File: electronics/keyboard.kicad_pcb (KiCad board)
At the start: 2 copper layers, 243 parts, among them CON1 AVR-ISP-6, J2 CONN_01X02_FEMALE, Q1 Q_NMOS_DGS, Q2 Q_NMOS_DGS, Q3 Q_PMOS_DGS, Q4 Q_NMOS_DGS, Q5 Q_PMOS_DGS, SW1 SW_DPST, SW10 SW_Push, SW11 SW_Push, SW12 SW_Push, SW13 SW_Push, SW14 SW_Push, SW15 SW_Push, SW16 SW_Push, SW17 SW_Push, SW18 SW_Push, SW19 SW_Push, SW2 SW_Push, SW20 SW_Push, SW21 SW_Push, SW22 SW_Push, SW23 SW_Push, SW24 SW_Push, SW25 SW_Push, SW26 SW_Push, SW27 SW_Push, SW28 SW_Push, SW29 SW_Push, SW3 SW_Push, SW30 SW_Push, SW31 SW_Push, SW32 SW_Push, SW33 SW_Push, SW34 SW_Push, SW35 SW_Push, SW36 SW_Push, SW37 SW_Push, SW38 SW_Push, SW39 SW_Push, SW4 SW_Push, SW40 SW_Push, SW41 SW_Push, SW42 SW_Push, SW43 SW_Push, SW44 SW_Push, SW45 SW_Push, SW46 SW_Push, SW47 SW_Push, SW48 SW_Push, SW49 SW_Push, SW5 SW_Push, SW50 SW_Push, SW51 SW_Push, SW52 SW_Push, SW53 SW_Push, SW54 SW_Push, SW55 SW_Push, SW56 SW_Push, SW57 SW_Push, SW58 SW_Push, SW59 SW_Push, SW6 SW_Push, SW60 SW_Push, SW61 SW_Push, SW62 SW_Push, SW63 SW_Push, SW64 SW_Push, SW65 SW_Push, SW66 SW_Push, SW67 SW_Push, SW68 SW_Push, SW69 SW_Push, SW7 SW_Push, SW70 SW_Push, SW71 SW_Push, SW72 SW_Push, SW73 SW_Push, SW74 SW_Push, SW75 SW_Push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

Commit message: Seperated elements in a sane way...
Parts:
- moved U2 181.8 mm to (325.1, 113.0)
- moved R15 176.2 mm to (340.4, 110.5)
- moved R18 161.5 mm to (340.4, 102.9)
- moved R17 161.5 mm to (349.2, 102.9)
- moved Q2 158.0 mm to (306.1, 124.5)
- moved R14 157.7 mm to (306.1, 129.5), turned to 180 degrees
- moved R16 157.4 mm to (304.8, 110.5)
- moved D1 156.7 mm to (350.5, 115.6)
- moved D2 156.7 mm to (350.5, 111.8)
- moved R5 143.5 mm to (301.0, 102.9)
- moved C9 142.2 mm to (323.9, 171.4)
- moved R13 126.4 mm to (308.6, 88.9)
- moved R8 117.4 mm to (302.3, 82.5)
- moved Q1 113.7 mm to (303.5, 99.1)
- moved R11 112.5 mm to (308.6, 78.7)
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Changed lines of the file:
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@@
     (links 407)
     (no_connects 407)
-    (area -421.280001 -139.340001 341.665001 243.975)
+    (area -421.280001 -139.340001 401.245001 243.975)
     (thickness 1.6)
     (drawings 0)
@@
   )
   (module Capacitors_SMD:C_0805_HandSoldering (layer F.Cu)
-    (at 187.96 129.54)
+    (at 323.85 171.45)
     (descr "Capacitor SMD 0805, hand soldering")
     (tags "capacitor 0805")
@@
   )
   (module LEDs:LED_0805 (layer F.Cu)
-    (at 200.66 161.29)
+    (at 350.52 115.57)
     (descr "LED 0805 smd package")
     (tags "LED led 0805 SMD smd SMT smt smdled SMDLED smtled SMTLED")
@@
   )
   (module LEDs:LED_0805 (layer F.Cu)
-    (at 200.66 157.48)
+    (at 350.52 111.76)
     (descr "LED 0805 smd package")
     (tags "LED led 0805 SMD smd SMT smt smdled SMDLED smtled SMTLED")
@@
   )
   (module TO_SOT_Packages_SMD:SC-59 (layer F.Cu)
-    (at 190.5 86.36)
+    (at 303.53 99.06)
     (descr "SC-59, https://lib.chipdip.ru/images/import_diod/original/SOT-23_SC-59.jpg")
     (tags SC-59)
@@
   )
   (module TO_SOT_Packages_SMD:SC-59 (layer F.Cu)
-    (at 152.4 87.63)
+    (at 306.07 124.46)
     (descr "SC-59, https://lib.chipdip.ru/images/import_diod/original/SOT-23_SC-59.jpg")
     (tags SC-59)
@@
   )
   (module Resistors_SMD:R_0805_HandSoldering (layer F.Cu)
-    (at 157.48 104.14)
+    (at 300.99 102.87)
     (descr "Resistor SMD 0805, hand soldering")
     (tags "resistor 0805")
@@
   )
   (module Resistors_SMD:R_0805_HandSoldering (layer F.Cu)
-    (at 196.85 81.28)
+    (at 306.07 102.87)
     (descr "Resistor SMD 0805, hand soldering")
     (tags "resistor 0805")
@@
   )
   (module Resistors_SMD:R_0805_HandSoldering (layer F.Cu)
-    (at 199.39 95.25)
+    (at 308.61 82.55)
     (descr "Resistor SMD 0805, hand soldering")
     (tags "resistor 0805")
@@
   )
   (module Resistors_SMD:R_0805_HandSoldering (layer F.Cu)
-    (at 185.42 93.98)
+    (at 302.26 82.55)
     (descr "Resistor SMD 0805, hand soldering")
     (tags "resistor 0805")
@@
   )
   (module Resistors_SMD:R_0805_HandSoldering (layer F.Cu)
-    (at 203.2 87.63)
+    (at 306.07 118.11)
     (descr "Resistor SMD 0805, hand soldering")
     (tags "resistor 0805")
@@
   )
   (module Resistors_SMD:R_0805_HandSoldering (layer F.Cu)
-    (at 207.01 107.95)
+    (at 302.26 78.74)
     (descr "Resistor SMD 0805, hand soldering")
     (tags "resistor 0805")
@@
   )
   (module Resistors_SMD:R_0805_HandSoldering (layer F.Cu)
-    (at 218.44 146.05)
+    (at 308.61 78.74)
     (descr "Resistor SMD 0805, hand soldering")
     (tags "resistor 0805")
@@
   )
   (module Resistors_SMD:R_0805_HandSoldering (layer F.Cu)
-    (at 212.09 146.05)
+    (at 302.26 88.9)
     (descr "Resistor SMD 0805, hand soldering")
     (tags "resistor 0805")
@@
   )
   (module Resistors_SMD:R_0805_HandSoldering (layer F.Cu)
-    (at 210.82 168.91)
+    (at 308.61 88.9)
     (descr "Resistor SMD 0805, hand soldering")
     (tags "resistor 0805")
@@
   )
   (module Resistors_SMD:R_0805_HandSoldering (layer F.Cu)
-    (at 149.86 151.13)
+    (at 306.07 129.54 180)
     (descr "Resistor SMD 0805, hand soldering")
     (tags "resistor 0805")
     (attr smd)
-    (fp_text reference R14 (at 0 -1.7) (layer F.SilkS)
+    (fp_text reference R14 (at 0 -1.7 180) (layer F.SilkS)
       (effects (font (size 1 1) (thickness 0.15)))
     )
-    (fp_text value 10k (at 0 1.75) (layer F.Fab)
+    (fp_text value 10k (at 0 1.75 180) (layer F.Fab)
       (effects (font (size 1 1) (thickness 0.15)))
     )
-    (fp_text user %R (at 0 -1.7) (layer F.Fab)
+    (fp_text user %R (at 0 -1.7 180) (layer F.Fab)
       (effects (font (size 1 1) (thickness 0.15)))
     )
@@
     (fp_line (start 2.35 0.9) (end 2.35 -0.9) (layer F.CrtYd) (width 0.05))
     (fp_line (start 2.35 0.9) (end -2.35 0.9) (layer F.CrtYd) (width 0.05))
-    (pad 1 smd rect (at -1.35 0) (size 1.5 1.3) (layers F.Cu F.Paste F.Mask)
+    (pad 1 smd rect (at -1.35 0 180) (size 1.5 1.3) (layers F.Cu F.Paste F.Mask)
       (net 3 +5V))
-    (pad 2 smd rect (at 1.35 0) (size 1.5 1.3) (layers F.Cu F.Paste F.Mask)
+    (pad 2 smd rect (at 1.35 0 180) (size 1.5 1.3) (layers F.Cu F.Paste F.Mask)
       (net 122 /PF1))
     (model Resistors_SMD.3dshapes/R_0805.wrl
@@
   )
   (module Resistors_SMD:R_0805_HandSoldering (layer F.Cu)
-    (at 168.91 151.13)
+    (at 340.36 110.49)
     (descr "Resistor SMD 0805, hand soldering")
     (tags "resistor 0805")
@@
   )
   (module Resistors_SMD:R_0805_HandSoldering (layer F.Cu)
-    (at 149.86 138.43)
+    (at 304.8 110.49)
     (descr "Resistor SMD 0805, hand soldering")
     (tags "resistor 0805")
@@
   )
   (module Resistors_SMD:R_0805_HandSoldering (layer F.Cu)
-    (at 194.31 148.59)
+    (at 349.25 102.87)
     (descr "Resistor SMD 0805, hand soldering")
     (tags "resistor 0805")
@@
   )
   (module Resistors_SMD:R_0805_HandSoldering (layer F.Cu)
-    (at 185.42 148.59)
+    (at 340.36 102.87)
     (descr "Resistor SMD 0805, hand soldering")
     (tags "resistor 0805")
@@
   )
   (module RF_Modules:RN42 (layer F.Cu)
-    (at 156.21 180.34)
+    (at 325.12 113.03)
     (descr "Class 2 Bluetooth Module with on-board antenna")
     (tags "Bluetooth Module")

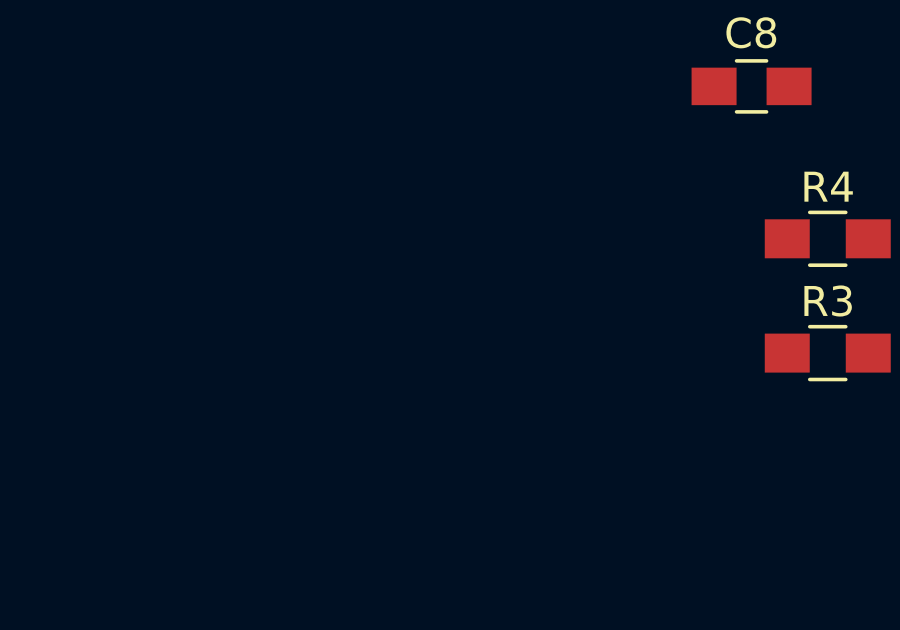
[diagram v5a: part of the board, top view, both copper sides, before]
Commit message: Updated the usb connector to micro usb at the momement because it is in the lib
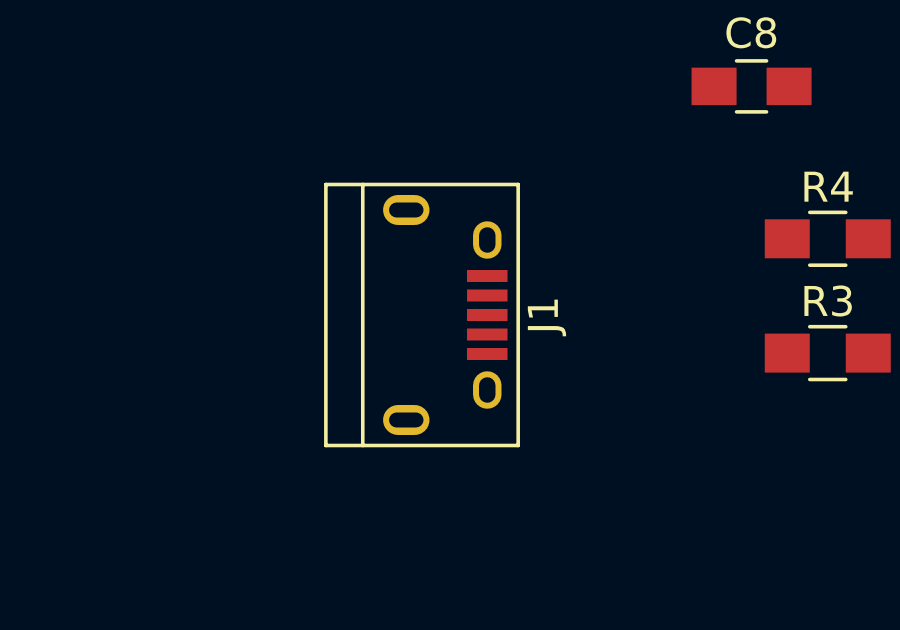
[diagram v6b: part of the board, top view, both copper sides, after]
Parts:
- added J1: USB_OTG, Connectors:USB_Micro-B, F.Cu at (295.9, 186.7)
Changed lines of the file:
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@@
 (kicad_pcb (version 4) (host pcbnew 4.0.6)
   (general
-    (links 407)
-    (no_connects 407)
-    (area -421.280001 -139.340001 401.245001 243.975)
+    (links 415)
+    (no_connects 415)
+    (area 0 0 0 0)
     (thickness 1.6)
     (drawings 0)
     (tracks 0)
     (zones 0)
-    (modules 243)
-    (nets 195)
+    (modules 244)
+    (nets 196)
   )
   (page A4)
@@
   (net 193 "Net-(U4-Pad3)")
   (net 194 "Net-(CON1-Pad2)")
+  (net 195 "Net-(J1-Pad4)")
   (net_class Default "This is the default net class."
     (clearance 0.2)
@@
     (add_net "Net-(D95-Pad2)")
     (add_net "Net-(D96-Pad2)")
+    (add_net "Net-(J1-Pad4)")
     (add_net "Net-(Q3-Pad2)")
     (add_net "Net-(Q4-Pad1)")
@@
     )
   )
+  (module Connectors:USB_Micro-B (layer F.Cu)
+    (at 295.91 186.69 270)
+    (descr "Micro USB Type B Receptacle")
+    (tags "USB USB_B USB_micro USB_OTG")
+    (attr smd)
+    (fp_text reference J1 (at 0 -3.24 270) (layer F.SilkS)
+      (effects (font (size 1 1) (thickness 0.15)))
+    )
+    (fp_text value USB_OTG (at 0 5.01 270) (layer F.Fab)
+      (effects (font (size 1 1) (thickness 0.15)))
+    )
+    (fp_line (start -4.6 -2.59) (end 4.6 -2.59) (layer F.CrtYd) (width 0.05))
+    (fp_line (start 4.6 -2.59) (end 4.6 4.26) (layer F.CrtYd) (width 0.05))
+    (fp_line (start 4.6 4.26) (end -4.6 4.26) (layer F.CrtYd) (width 0.05))
+    (fp_line (start -4.6 4.26) (end -4.6 -2.59) (layer F.CrtYd) (width 0.05))
+    (fp_line (start -4.35 4.03) (end 4.35 4.03) (layer F.SilkS) (width 0.12))
+    (fp_line (start -4.35 -2.38) (end 4.35 -2.38) (layer F.SilkS) (width 0.12))
+    (fp_line (start 4.35 -2.38) (end 4.35 4.03) (layer F.SilkS) (width 0.12))
+    (fp_line (start 4.35 2.8) (end -4.35 2.8) (layer F.SilkS) (width 0.12))
+    (fp_line (start -4.35 4.03) (end -4.35 -2.38) (layer F.SilkS) (width 0.12))
+    (pad 1 smd rect (at -1.3 -1.35) (size 1.35 0.4) (layers F.Cu F.Paste F.Mask)
+      (net 10 /VBUS))
+    (pad 2 smd rect (at -0.65 -1.35) (size 1.35 0.4) (layers F.Cu F.Paste F.Mask)
+      (net 133 /DMINUS))
+    (pad 3 smd rect (at 0 -1.35) (size 1.35 0.4) (layers F.Cu F.Paste F.Mask)
+      (net 131 /DPLUS))
+    (pad 4 smd rect (at 0.65 -1.35) (size 1.35 0.4) (layers F.Cu F.Paste F.Mask)
+      (net 195 "Net-(J1-Pad4)"))
+    (pad 5 smd rect (at 1.3 -1.35) (size 1.35 0.4) (layers F.Cu F.Paste F.Mask)
+      (net 2 GND))
+    (pad 6 thru_hole oval (at -2.5 -1.35) (size 0.95 1.25) (drill oval 0.55 0.85) (layers *.Cu *.Mask)
+      (net 2 GND))
+    (pad 6 thru_hole oval (at 2.5 -1.35) (size 0.95 1.25) (drill oval 0.55 0.85) (layers *.Cu *.Mask)
+      (net 2 GND))
+    (pad 6 thru_hole oval (at -3.5 1.35) (size 1.55 1) (drill oval 1.15 0.5) (layers *.Cu *.Mask)
+      (net 2 GND))
+    (pad 6 thru_hole oval (at 3.5 1.35) (size 1.55 1) (drill oval 1.15 0.5) (layers *.Cu *.Mask)
+      (net 2 GND))
+  )
 )

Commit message: Started working on the switches placements
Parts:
- moved SW20 447.9 mm to (309.9, 185.4)
- moved SW57 443.6 mm to (348.0, 128.3)
- moved SW2 423.5 mm to (183.7, 195.6)
- moved SW23 393.6 mm to (328.9, 90.2)
- moved SW53 385.5 mm to (290.9, 90.2)
- moved SW15 381.2 mm to (348.0, 90.2)
- moved SW14 373.3 mm to (348.0, 147.3)
- moved SW39 371.8 mm to (348.0, 166.4)
- moved SW13 359.2 mm to (348.0, 109.3)
- moved SW46 353.3 mm to (348.0, 185.4)
- moved SW37 351.5 mm to (328.9, 166.4)
- moved SW41 332.9 mm to (328.9, 185.4)
- moved SW17 329.0 mm to (290.8, 185.4)
- moved SW32 309.1 mm to (310.0, 90.2)
- moved SW45 285.9 mm to (271.8, 185.4)
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
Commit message: Worked on Placement changed the mothod to do it...
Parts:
- SW2, SW6, SW7: moved to F.Cu
- moved SW47 558.0 mm to (247.7, 114.3)
- moved SW70 552.4 mm to (266.7, 114.3)
- moved SW71 542.5 mm to (285.8, 114.3)
- moved SW44 541.8 mm to (209.6, 114.3)
- moved SW72 539.0 mm to (304.8, 114.3)
- moved SW73 535.5 mm to (323.9, 114.3)
- moved SW86 442.1 mm to (304.8, 209.6)
- moved SW78 442.1 mm to (323.9, 133.3)
- moved SW22 415.3 mm to (276.2, 152.4)
- moved SW19 414.2 mm to (304.8, 190.5)
- moved SW49 403.6 mm to (285.8, 209.6)
- moved SW12 401.7 mm to (64.3, 209.6)
- moved SW27 400.3 mm to (252.4, 190.5)
- moved SW74 397.5 mm to (190.5, 114.3)
- moved SW85 380.9 mm to (266.7, 209.6)
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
